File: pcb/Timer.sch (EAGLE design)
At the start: 43 parts, among them J1 PWR, J2 EXT, J3 ISP, J4 DCF77, J5 DISP1, J6 DISP2, J7 DISP3, J8 DISP4, U1 ATTINY24SSU, U2 SCT2024CSOG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

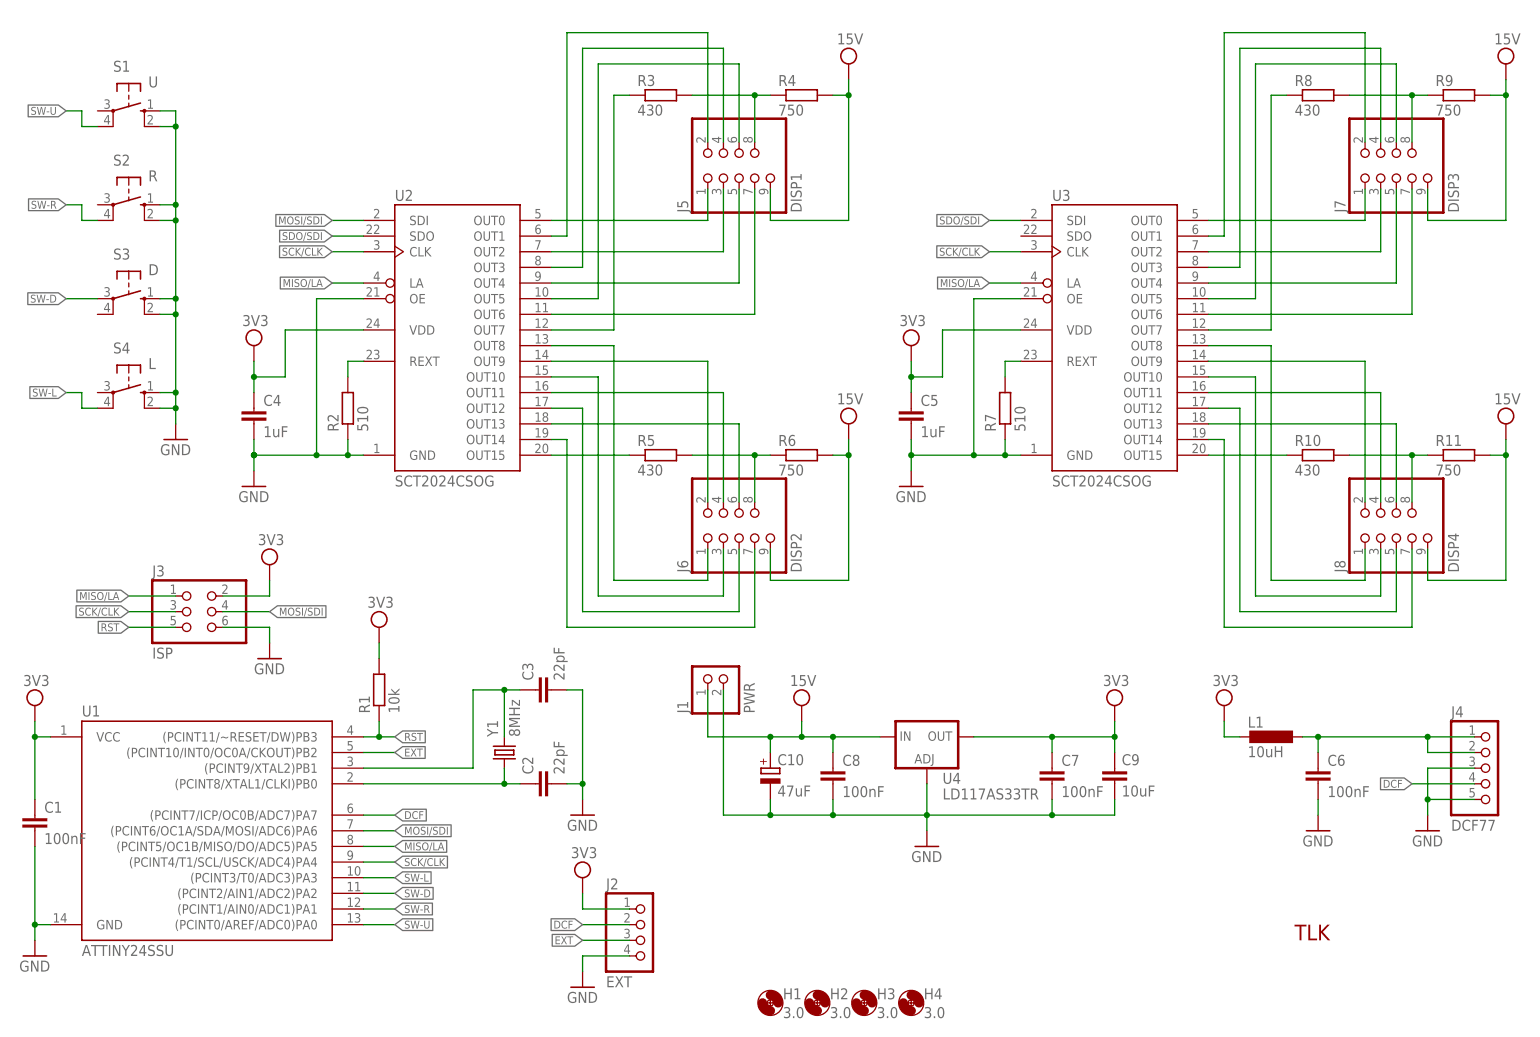
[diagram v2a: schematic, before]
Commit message: Fix errors, move components to a common library
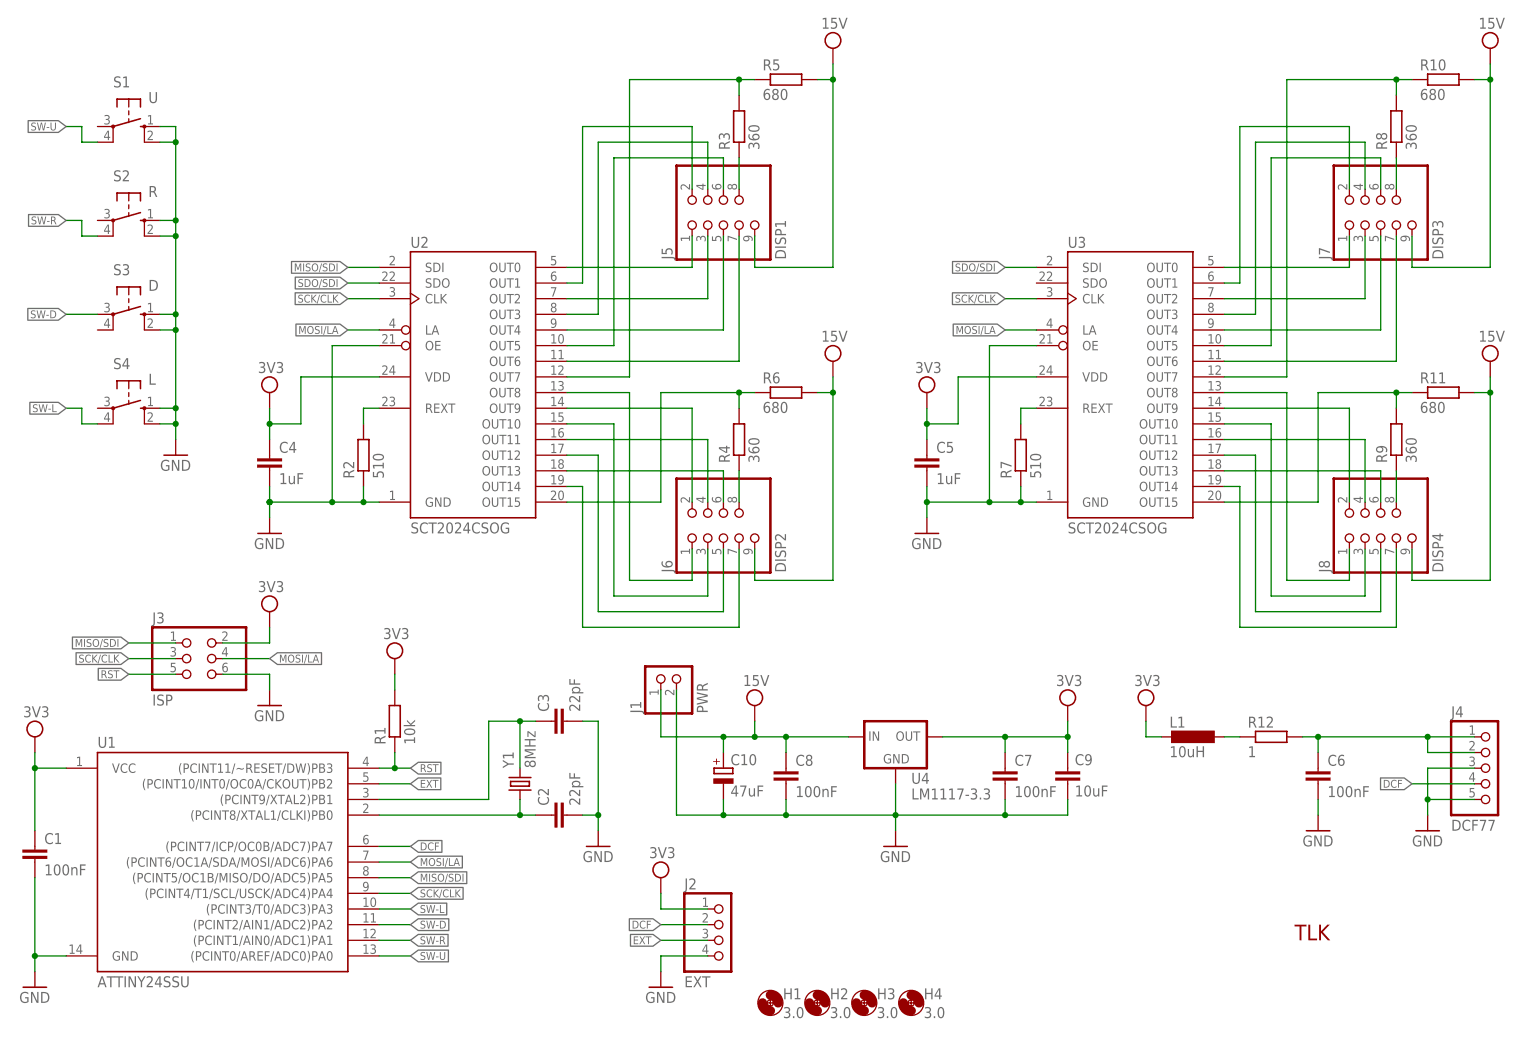
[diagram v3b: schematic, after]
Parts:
- added R12: 1, Timer:R-EUR0805
- C1, C2, C3, C4, C5, C6, C7, C8, C9: device .rcl:C-EUC0805 -> Timer:C-EUC0805
- C10: device .rcl:CPOL-EUE2.5 -> Timer:CPOL-EUE2.5
- J1: device .pinhead:PINHD-1X2/90 -> Timer:PINHD-1X2/90
- J2: device .pinhead:PINHD-1X4/90 -> Timer:PINHD-1X4/90
- J3: device .pinhead:PINHD-2X3/90 -> Timer:PINHD-2X3/90
- J4: device .pinhead:PINHD-1X5/90 -> Timer:PINHD-1X5/90
- J5, J6, J7, J8: device .pinhead:PINHD-2X4/5/90 -> Timer:PINHD-2X4/5/90
- L1: device .rcl:L-EUL0805 -> Timer:L-EUL0805
- R1, R2, R7: device .rcl:R-EUR0805 -> Timer:R-EUR0805
- R10, R5: value 430 -> 680; device .rcl:R-EUR1206 -> Timer:R-EUR1206
- R11, R6: value 750 -> 680; device .rcl:R-EUR1206 -> Timer:R-EUR1206
- R3, R8: value 430 -> 360; device .rcl:R-EUR1206 -> Timer:R-EUR1206
- R4, R9: value 750 -> 360; device .rcl:R-EUR1206 -> Timer:R-EUR1206
- S1, S2, S3, S4: device .switch:TACT -> Timer:TACT
- U1: device .atmel:ATTINY24SSU -> Timer:ATTINY24SSU
- U2, U3: device .starchips:SCT2024CSOG -> Timer:SCT2024CSOG
- U4: value LD117AS33TR -> LM1117-3.3; device .v-reg:LD117AS33TR -> Timer:LM1117-3.3
- Y1: device .crystal:CRYSTALHC49UP -> Timer:CRYSTALHC49UP
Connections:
- removed net MISO/LA: J3.1, U1.(PCINT5/OC1B/MISO/DO/ADC5)PA5, U2.LA, U3.LA
- removed net MOSI/SDI: J3.4, U1.(PCINT6/OC1A/SDA/MOSI/ADC6)PA6, U2.SDI
- new net MISO/SDI: J3.1, U1.(PCINT5/OC1B/MISO/DO/ADC5)PA5, U2.SDI
- new net MOSI/LA: J3.4, U1.(PCINT6/OC1A/SDA/MOSI/ADC6)PA6, U2.LA, U3.LA
- new net N$29: L1.1, R12.1
- net GND: now also U4.GND; no longer U4.ADJ
- net N$10: now also R3.1; no longer R3.2, R4.1
- net N$12: now also R3.2, R5.1; no longer R3.1
- net N$21: now also R8.1; no longer R8.2, R9.1
- net N$23: now also R10.1, R8.2; no longer R8.1
- net N$27: now also R11.1, R9.2; no longer R10.1
- net N$28: now also R9.1; no longer R10.2, R11.1
- net N$3: now also R12.2; no longer L1.1
- net N$34: now also R4.1; no longer R5.2, R6.1
- net N$41: now also R4.2, R6.1; no longer R5.1
- net VDD: now also R10.2, R5.2; no longer R4.2, R9.2
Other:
- moved on the sheet: C1, C10, C2, C3, C4, C5, C7, C8, C9, J1, J2, J3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

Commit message: Change C6 value
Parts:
- C6: value 100nF -> 10uF
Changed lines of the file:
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@@
 <part name="GND7" library="supply1" library_urn="urn:adsk.eagle:library:371" deviceset="GND" device=""/>
 <part name="L1" library="Timer" deviceset="L-EU" device="L0805" value="10uH"/>
-<part name="C6" library="Timer" deviceset="C-EU" device="C0805" value="100nF"/>
+<part name="C6" library="Timer" deviceset="C-EU" device="C0805" value="10uF"/>
 <part name="GND8" library="supply1" library_urn="urn:adsk.eagle:library:371" deviceset="GND" device=""/>
 <part name="C9" library="Timer" deviceset="C-EU" device="C0805" value="10uF"/>
